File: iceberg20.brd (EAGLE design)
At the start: 86 parts, among them M0:+ TPB1,27, M0:- TPB1,27, M0:C1 10nF, M0:C2 220nF, M0:C3 100nF, M0:C4 100uF, M0:C5 1nF, M0:C6 100nF, M0:D1 1N4148W, M0:D2 1N4148W, M0:EN TPB1,27, M0:I TPB1,27, M0:IC1 L6205N, M0:IC2 ACS712, M0:IN1 TPB1,27, M0:IN2 TPB1,27, M0:R1 100R, M0:R2 100k, M0:R3 10k, M0:VS TPB1,27, M1:+ TPB1,27, M1:- TPB1,27, M1:C1 10nF, M1:C2 220nF, M1:C3 100nF, M1:C4 100uF, M1:C5 1nF, M1:C6 100nF, M1:D1 1N4148W, M1:D2 1N4148W, M1:EN TPB1,27, M1:I TPB1,27, M1:IC1 L6205N, M1:IC2 ACS712, M1:IN1 TPB1,27, M1:IN2 TPB1,27, M1:R1 100R, M1:R2 100k, M1:R3 10k, M1:VS TPB1,27, M2:+ TPB1,27, M2:- TPB1,27, M2:C1 10nF, M2:C2 220nF, M2:C3 100nF, M2:C4 100uF, M2:C5 1nF, M2:C6 100nF, M2:D1 1N4148W, M2:D2 1N4148W, M2:EN TPB1,27, M2:I TPB1,27, M2:IC1 L6205N, M2:IC2 ACS712, M2:IN1 TPB1,27, M2:IN2 TPB1,27, M2:R1 100R, M2:R2 100k, M2:R3 10k, M2:VS TPB1,27, M3:+ TPB1,27, M3:- TPB1,27, M3:C1 10nF, M3:C2 220nF, M3:C3 100nF, M3:C4 100uF, M3:C5 1nF, M3:C6 100nF, M3:D1 1N4148W, M3:D2 1N4148W, M3:EN TPB1,27, M3:I TPB1,27, M3:IC1 L6205N, M3:IC2 ACS712, M3:IN1 TPB1,27, M3:IN2 TPB1,27, M3:R1 100R, M3:R2 100k, M3:R3 10k, M3:VS TPB1,27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

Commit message: Fixes
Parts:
- removed P1:J1: 1X2-3.5MM, adafruit:1X2-3.5MM
- removed P1:S1: SWITCH, Custom-Parts:100SP1T1B4M2QE
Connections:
- removed net P1:N$1: P1:J1.2, P1:S1.2
- net +12V: no longer P1:S1.1
- net GND: no longer P1:J1.1
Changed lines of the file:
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@@
 <?xml version="1.0" encoding="utf-8"?>
 <!DOCTYPE eagle SYSTEM "eagle.dtd">
-<eagle version="9.4.2">
+<eagle version="9.4.1">
 <drawing>
 <settings>
@@
 <attribute name="VALUE" x="-13.335" y="-328.422" size="0.0254" layer="27"/>
 </element>
-<element name="P1:J1" library="adafruit" library_urn="urn:adsk.eagle:library:420" package="1X2-3.5MM" package3d_urn="urn:adsk.eagle:package:6240635/1" value="1X2-3.5MM" x="-17.78" y="-325.12" smashed="yes">
-<attribute name="NAME" x="-14.78" y="-320.12" size="1.27" layer="25" rot="R180"/>
-</element>
-<element name="P1:S1" library="Custom-Parts" library_urn="urn:adsk.eagle:library:10181880" package="100SP1T1B4M2QE" package3d_urn="urn:adsk.eagle:package:10181901/2" value="SWITCH" x="-12.7" y="-335.915" smashed="yes">
-<attribute name="NAME" x="-20.32" y="-329.565" size="1.27" layer="25" align="top-left"/>
-<attribute name="VALUE" x="-5.08" y="-329.565" size="1.27" layer="27" align="top-right"/>
-</element>
 </elements>
 <signals>
@@
 <wire x1="183.337703125" y1="-53.63306875" x2="183.337703125" y2="-55.245" width="0.1524" layer="1"/>
 <via x="183.337703125" y="-55.245" extent="1-16" drill="0.35"/>
-<contactref element="P1:J1" pad="1"/>
 <wire x1="-4.39274375" y1="-187.980509375" x2="-11.4" y2="-181.833709375" width="0" layer="19" extent="1-1"/>
 <wire x1="-8.8082" y1="-169.413109375" x2="-11.4" y2="-181.833709375" width="0" layer="19" extent="1-1"/>
@@
 <wire x1="0.9398" y1="-25.439675" x2="0.9398" y2="-33.059675" width="0" layer="19" extent="1-1"/>
 <wire x1="3.4798" y1="-25.439675" x2="0.9398" y2="-25.439675" width="0" layer="19" extent="1-1"/>
-<wire x1="-15.98" y1="-325.12" x2="-4.39274375" y2="-187.980509375" width="0" layer="19" extent="1-1"/>
 <wire x1="161.645096875" y1="-47.9298" x2="9.42016875" y2="-47.95180625" width="0" layer="19" extent="1-1"/>
 <wire x1="161.645096875" y1="-53.0098" x2="161.645096875" y2="-47.9298" width="0" layer="19" extent="1-1"/>
@@
 <signal name="+12V">
 <contactref element="F1:F1" pad="2"/>
-<contactref element="P1:S1" pad="1"/>
-<wire x1="11.844865625" y1="-66.79660625" x2="-17.4" y2="-335.915" width="0" layer="19" extent="1-1"/>
 </signal>
 <signal name="EN1">
@@
 <wire x1="5.7714" y1="-164.536309375" x2="-1.8486" y2="-164.536309375" width="0" layer="19" extent="1-1"/>
 </signal>
-<signal name="P1:N$1">
-<contactref element="P1:J1" pad="2"/>
-<contactref element="P1:S1" pad="2"/>
-<wire x1="-19.48" y1="-325.12" x2="-12.7" y2="-335.915" width="0" layer="19" extent="1-1"/>
-</signal>
 </signals>

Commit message: + sch (Power)
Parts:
- added P1:R1: 100k, iceberg20:R0805
- added P1:S1: SWITCH, iceberg20:1801.2106
- added P1:T1: AOD403, iceberg20:TO252
- added P1:U$1: TERMINAL-2, iceberg20:LIB_WECO121
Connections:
- new net P1:+12V: P1:T1.2
- new net P1:N$1: P1:S1.1, P1:U$1.P2
- new net P1:N$2: P1:S1.2, P1:T1.3
- new net P1:N$4: P1:R1.2, P1:T1.1
- net GND: now also P1:R1.1, P1:U$1.P1
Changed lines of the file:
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@@
 <?xml version="1.0" encoding="utf-8"?>
 <!DOCTYPE eagle SYSTEM "eagle.dtd">
-<eagle version="9.4.1">
+<eagle version="9.4.2">
 <drawing>
 <settings>
@@
 <attribute name="VALUE" x="-13.335" y="-328.422" size="0.0254" layer="27"/>
 </element>
+<element name="P1:S1" library="iceberg20" package="1801.2106" value="SWITCH" x="-21.59" y="-318.135" smashed="yes">
+<attribute name="BESTAND" value="1" x="-21.59" y="-318.135" size="1.778" layer="27" display="off"/>
+<attribute name="HERSTELLER" value="Marquardt" x="-21.59" y="-318.135" size="1.778" layer="27" display="off"/>
+<attribute name="HERSTELLER-NR" value="1801.2106" x="-21.59" y="-318.135" size="1.778" layer="27" display="off"/>
+<attribute name="NAME" x="-28.575" y="-306.705" size="1.778" layer="25" ratio="10"/>
+<attribute name="SUPPLIER" value="Bürklin" x="-21.59" y="-318.135" size="1.778" layer="27" display="off"/>
+<attribute name="SUPPLIER-NR" value="11G2420" x="-21.59" y="-318.135" size="1.778" layer="27" display="off"/>
+<attribute name="VALUE" x="-27.305" y="-327.025" size="1.778" layer="27" ratio="10"/>
+</element>
+<element name="P1:T1" library="iceberg20" package="TO252" package3d_urn="urn:adsk.eagle:package:12893169/1" value="AOD403" x="-35.56" y="-321.945" smashed="yes">
+<attribute name="BESTAND" value="0" x="-35.56" y="-321.945" size="1.778" layer="27" display="off"/>
+<attribute name="HERSTELLER" value="Alpha &amp; Omega" x="-35.56" y="-321.945" size="1.778" layer="27" display="off"/>
+<attribute name="HERSTELLER-NR" value="AOD403" x="-35.56" y="-321.945" size="1.778" layer="27" display="off"/>
+<attribute name="NAME" x="-35.56" y="-317.05" size="1.27" layer="25" align="bottom-center"/>
+<attribute name="SUPPLIER" value="Reichelt" x="-35.56" y="-321.945" size="1.778" layer="27" display="off"/>
+<attribute name="SUPPLIER-NR" value="AO D403" x="-35.56" y="-321.945" size="1.778" layer="27" display="off"/>
+<attribute name="VALUE" x="-35.56" y="-326.84" size="1.27" layer="27" align="top-center"/>
+</element>
+<element name="P1:U$1" library="iceberg20" package="LIB_WECO121" value="TERMINAL-2" x="-49.53" y="-322.58" smashed="yes">
+<attribute name="BESTAND" value="" x="-49.53" y="-322.58" size="1.778" layer="27" display="off"/>
+<attribute name="HERSTELLER" value="Weco" x="-49.53" y="-322.58" size="1.778" layer="27" display="off"/>
+<attribute name="HERSTELLER-NR" value="20806102 121-M-121/02-K" x="-49.53" y="-322.58" size="1.778" layer="27" display="off"/>
+<attribute name="NAME" x="-52.0973625" y="-318.4248625" size="0.6096" layer="25" font="vector" ratio="20"/>
+<attribute name="SUPPLIER" value="Bürklin" x="-49.53" y="-322.58" size="1.778" layer="27" display="off"/>
+<attribute name="SUPPLIER-NR" value="47F1100" x="-49.53" y="-322.58" size="1.778" layer="27" display="off"/>
+<attribute name="VALUE" x="-52.026596875" y="-328.2283" size="0.6096" layer="27" font="vector" ratio="20"/>
+</element>
+<element name="P1:R1" library="iceberg20" package="R0805" package3d_urn="urn:adsk.eagle:package:23553/2" value="100k" x="-50.165" y="-332.105" smashed="yes">
+<attribute name="BESTAND" value="-" x="-50.165" y="-332.105" size="1.778" layer="27" display="off"/>
+<attribute name="HERSTELLER" value="-" x="-50.165" y="-332.105" size="1.778" layer="27" display="off"/>
+<attribute name="HERSTELLER-NR" value="-" x="-50.165" y="-332.105" size="1.778" layer="27" display="off"/>
+<attribute name="NAME" x="-50.8" y="-330.835" size="1.27" layer="25"/>
+<attribute name="SUPPLIER" value="-" x="-50.165" y="-332.105" size="1.778" layer="27" display="off"/>
+<attribute name="SUPPLIER-NR" value="-" x="-50.165" y="-332.105" size="1.778" layer="27" display="off"/>
+<attribute name="TOLERANZ" value="5%" x="-50.165" y="-332.105" size="1.778" layer="27" display="off"/>
+<attribute name="VALUE" x="-50.8" y="-334.645" size="1.27" layer="27"/>
+</element>
 </elements>
 <signals>
@@
 <wire x1="183.337703125" y1="-53.63306875" x2="183.337703125" y2="-55.245" width="0.1524" layer="1"/>
 <via x="183.337703125" y="-55.245" extent="1-16" drill="0.35"/>
+<contactref element="P1:U$1" pad="P1"/>
+<contactref element="P1:R1" pad="1"/>
 <wire x1="-4.39274375" y1="-187.980509375" x2="-11.4" y2="-181.833709375" width="0" layer="19" extent="1-1"/>
 <wire x1="-8.8082" y1="-169.413109375" x2="-11.4" y2="-181.833709375" width="0" layer="19" extent="1-1"/>
@@
 <wire x1="0.9398" y1="-25.439675" x2="0.9398" y2="-33.059675" width="0" layer="19" extent="1-1"/>
 <wire x1="3.4798" y1="-25.439675" x2="0.9398" y2="-25.439675" width="0" layer="19" extent="1-1"/>
+<wire x1="-44.45" y1="-322.58" x2="-4.39274375" y2="-187.980509375" width="0" layer="19" extent="1-1"/>
+<wire x1="-51.115" y1="-332.105" x2="-44.45" y2="-322.58" width="0" layer="19" extent="1-1"/>
 <wire x1="161.645096875" y1="-47.9298" x2="9.42016875" y2="-47.95180625" width="0" layer="19" extent="1-1"/>
 <wire x1="161.645096875" y1="-53.0098" x2="161.645096875" y2="-47.9298" width="0" layer="19" extent="1-1"/>
@@
 <wire x1="5.7714" y1="-164.536309375" x2="-1.8486" y2="-164.536309375" width="0" layer="19" extent="1-1"/>
 </signal>
+<signal name="P1:N$1">
+<contactref element="P1:U$1" pad="P2"/>
+<contactref element="P1:S1" pad="1"/>
+<wire x1="-21.59" y1="-318.2112" x2="-49.53" y2="-322.58" width="0" layer="19" extent="1-1"/>
+</signal>
+<signal name="P1:N$2">
+<contactref element="P1:S1" pad="2"/>
+<contactref element="P1:T1" pad="3"/>
+<wire x1="-21.59" y1="-310.635" x2="-32.9857" y2="-321.945" width="0" layer="19" extent="1-1"/>
+</signal>
+<signal name="P1:N$4">
+<contactref element="P1:T1" pad="1"/>
+<contactref element="P1:R1" pad="2"/>
+<wire x1="-39.9057" y1="-319.655" x2="-49.215" y2="-332.105" width="0" layer="19" extent="1-1"/>
+</signal>
+<signal name="P1:+12V">
+<contactref element="P1:T1" pad="2"/>
+</signal>
 </signals>

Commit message: ultimate merge yeah!
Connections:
- net +12V renamed F1:IN
- removed net GND: F1:LED2.C, M0:C3.2, M0:C4.-, M0:C5.1, M0:C6.1, M0:IC1.15, M0:IC1.16, M0:IC1.3, M0:IC1.5, M0:IC1.6, M0:IC1.8, M0:IC2.5, M0:R3.1, M1:C3.2, M1:C4.-, M1:C5.1, M1:C6.1, M1:IC1.15, M1:IC1.16, M1:IC1.3, M1:IC1.5, M1:IC1.6, M1:IC1.8, M1:IC2.5, M1:R3.1, M2:C3.2, M2:C4.-, M2:C5.1, M2:C6.1, M2:IC1.15, M2:IC1.16, M2:IC1.3, M2:IC1.5, M2:IC1.6, M2:IC1.8, M2:IC2.5, M2:R3.1, M3:C3.2, M3:C4.-, M3:C5.1, M3:C6.1, M3:IC1.15, M3:IC1.16, M3:IC1.3, M3:IC1.5, M3:IC1.6, M3:IC1.8, M3:IC2.5, M3:R3.1, P1:R1.1, P1:U$1.P1
- new net F1:GND: F1:LED2.C
- new net M0:GND: M0:C3.2, M0:C4.-, M0:C5.1, M0:C6.1, M0:IC1.15, M0:IC1.16, M0:IC1.3, M0:IC1.5, M0:IC1.6, M0:IC1.8, M0:IC2.5, M0:R3.1
- new net M1:GND: M1:C3.2, M1:C4.-, M1:C5.1, M1:C6.1, M1:IC1.15, M1:IC1.16, M1:IC1.3, M1:IC1.5, M1:IC1.6, M1:IC1.8, M1:IC2.5, M1:R3.1
- new net M2:GND: M2:C3.2, M2:C4.-, M2:C5.1, M2:C6.1, M2:IC1.15, M2:IC1.16, M2:IC1.3, M2:IC1.5, M2:IC1.6, M2:IC1.8, M2:IC2.5, M2:R3.1
- new net M3:GND: M3:C3.2, M3:C4.-, M3:C5.1, M3:C6.1, M3:IC1.15, M3:IC1.16, M3:IC1.3, M3:IC1.5, M3:IC1.6, M3:IC1.8, M3:IC2.5, M3:R3.1
- new net P1:GND: P1:R1.1, P1:U$1.P1
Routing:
- net GND: track 4.73 -> 0.00 mm, vias 3 -> 0

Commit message: Fehlerbehebung
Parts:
- moved M3:VS 447.1 mm to (-19.1, 119.4)
- moved M3:IN1 424.2 mm to (-69.8, 113.0)
- moved M2:VS 417.9 mm to (-19.1, 95.2)
- moved M3:IN2 405.3 mm to (-77.5, 113.0)
- moved M2:IN1 395.3 mm to (-69.8, 88.9)
- moved M3:EN 386.6 mm to (-85.1, 113.0)
- moved M2:IN2 376.5 mm to (-77.5, 88.9)
- moved M1:IN1 367.2 mm to (-69.8, 64.8)
- moved M3:I 366.4 mm to (-34.3, 119.4)
- moved M1:IN2 364.1 mm to (-77.5, 64.8)
- moved M1:EN 362.2 mm to (-85.1, 64.8)
- moved M0:VS 359.5 mm to (-19.1, 47.0)
- moved M2:EN 357.9 mm to (-85.1, 88.9)
- moved M3:- 345.8 mm to (-29.2, 119.4)
- moved M1:VS 340.6 mm to (-19.1, 71.1)
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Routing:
- net M1:N$9: track 28.2 -> 0.00 mm
- net M1:FILTER: track 2.92 -> 0.00 mm
- net EN1: track 2.45 -> 0.00 mm
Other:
- board outline added: 160 x 100 mm

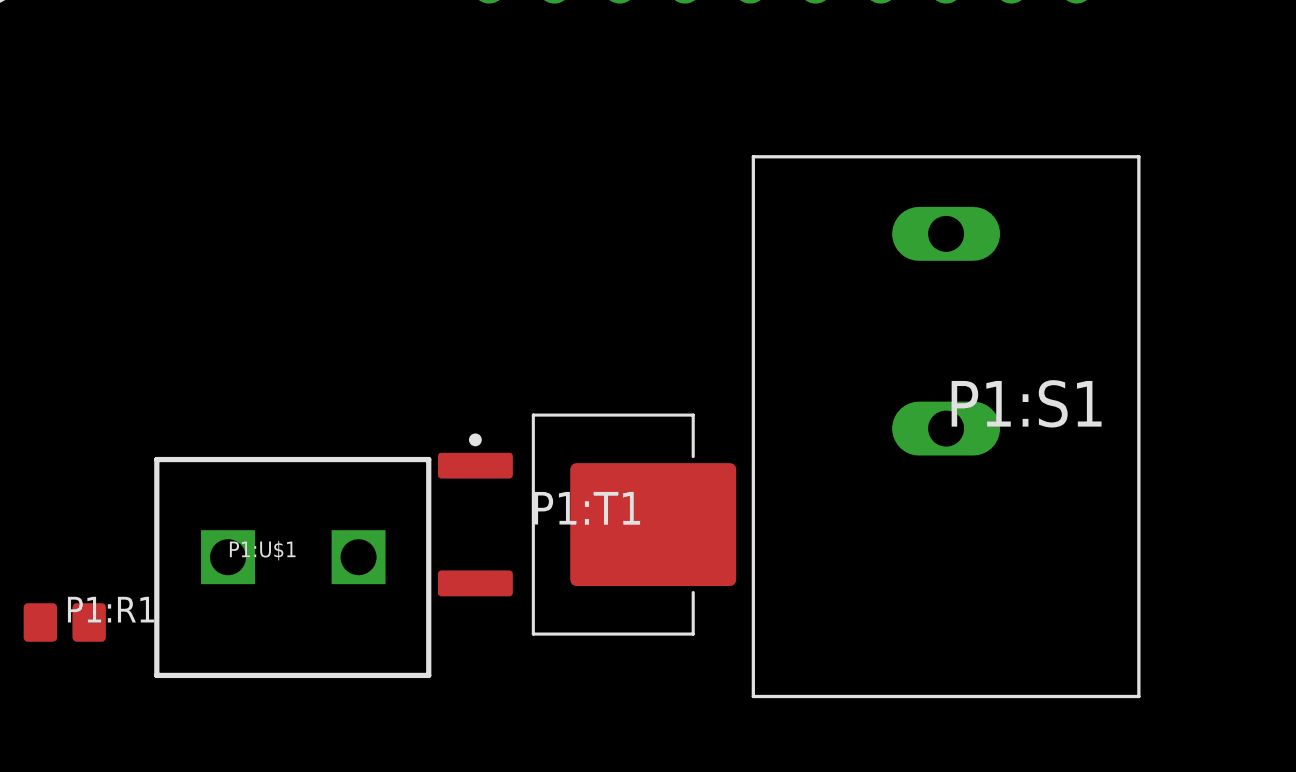
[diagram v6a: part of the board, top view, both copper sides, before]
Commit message: + sch(Sensoren, Ein/Ausgabe)
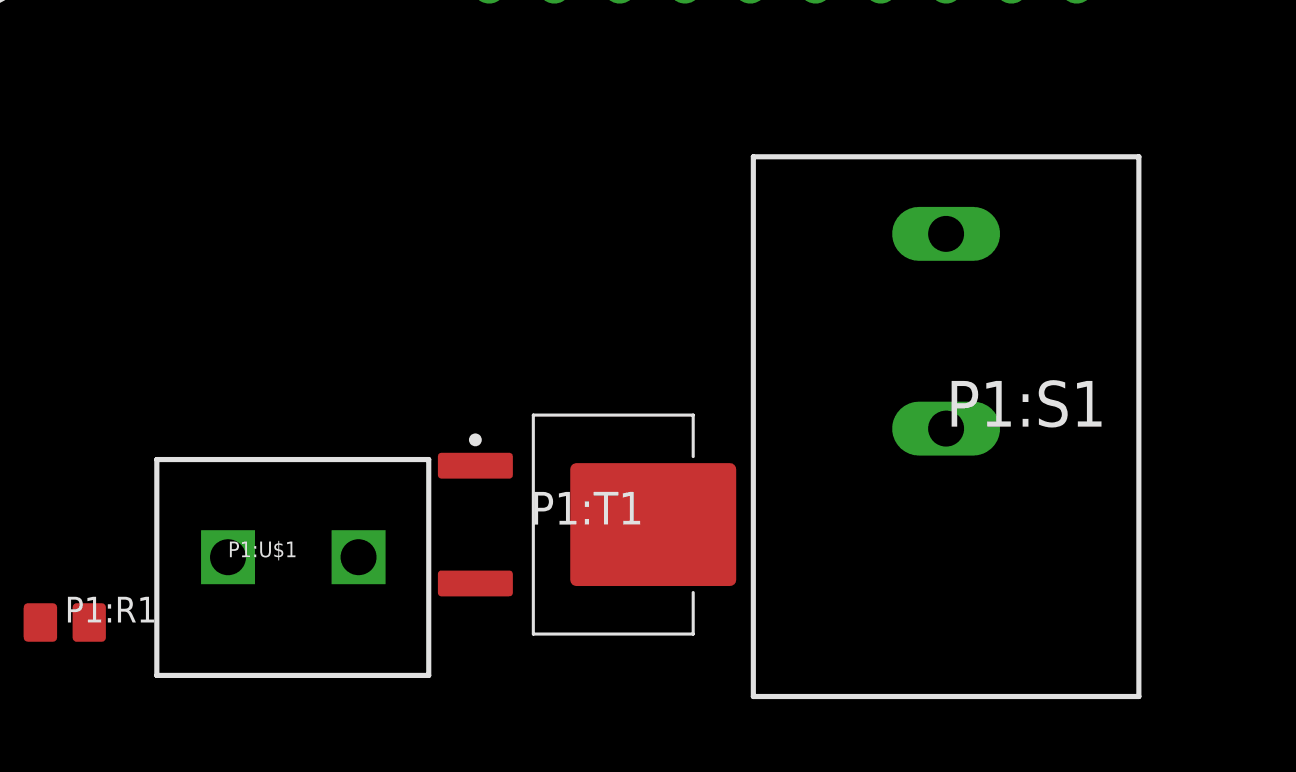
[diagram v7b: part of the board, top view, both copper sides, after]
